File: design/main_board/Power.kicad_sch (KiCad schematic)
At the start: 45 parts, among them SW301 SW_SPDT, U301 AP2138N-3.3TRG1, U302 TPS61235P, U303 AAT3693

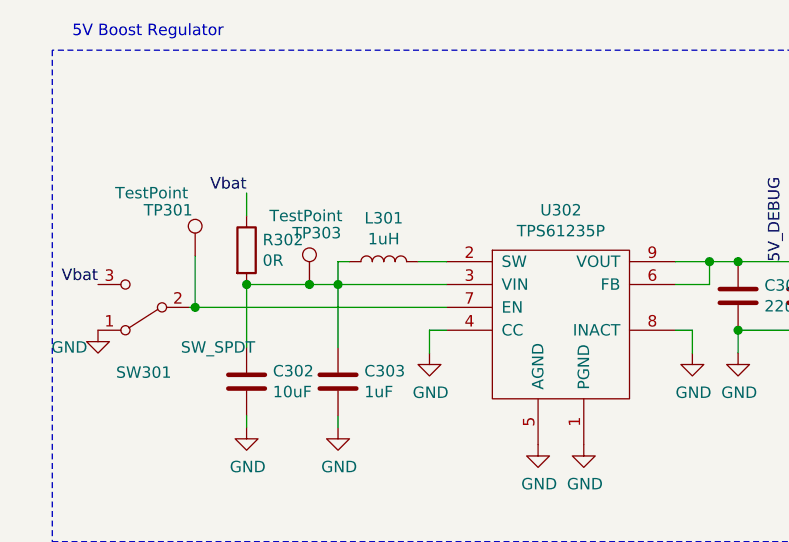
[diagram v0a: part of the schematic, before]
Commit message: Created esp32 footprint and symbol
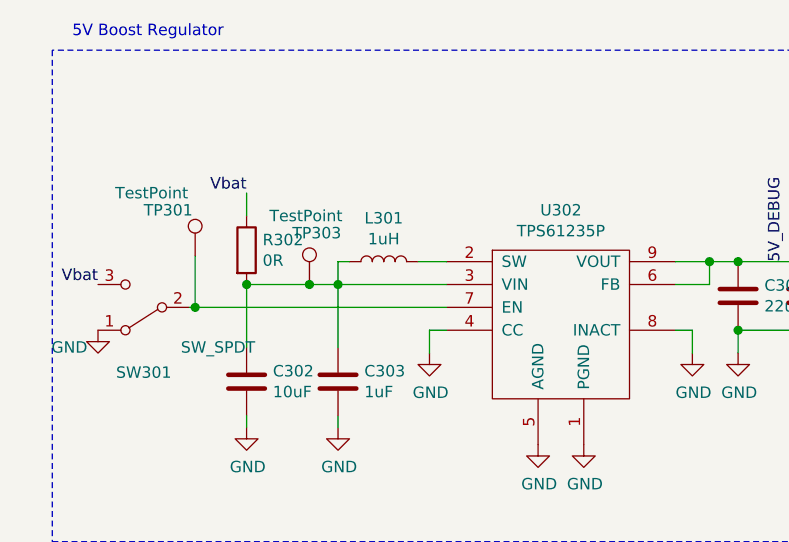
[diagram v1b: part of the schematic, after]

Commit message: Schematic almost finished
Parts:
- removed R301, R304, R306: 0R, Resistor_SMD:R_0603_1608Metric, symbol Device:R
- removed R302, R303, R307: 0R, Resistor_SMD:R_1206_3216Metric, symbol Device:R
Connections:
- net 3V3_DEBUG is gone; now on net +3V3: C305.1, D302.2 (A), TP304.1, U301.2 (Vout)
- net 5V_DEBUG is gone; now on net +5V: C304.1, C306.1, C307.1, D301.2 (A), TP305.1, U302.6 (FB), U302.9 (VOUT)
- net +5V: now also C301.1, TP302.1, U301.3 (Vin)
- net VBAT_SENSE: now also C302.1, C303.1, L301.1, TP303.1, U302.3 (VIN)
- net VBUS: now also C308.1, D303.2 (A), D304.2 (A), R313.1, TP306.1, U303.1 (VIN), U303.4 (EN)
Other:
- note removed: "Enable Resistor"

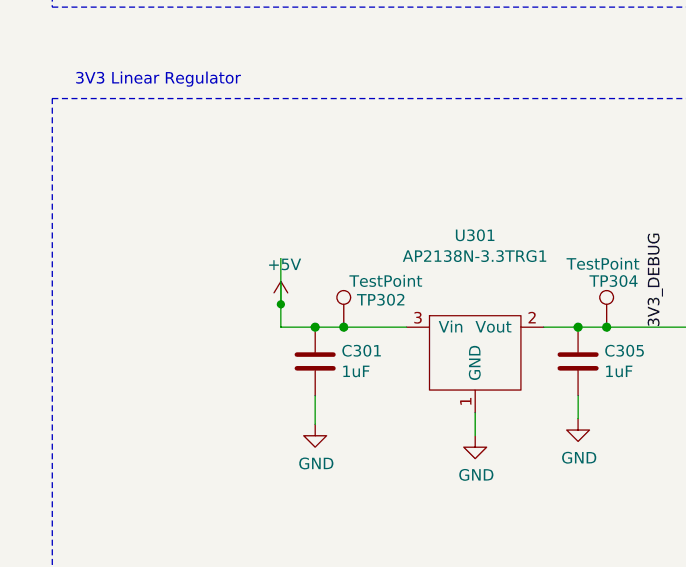
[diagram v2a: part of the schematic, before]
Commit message: Added new firmware hello world for ESP32-S3
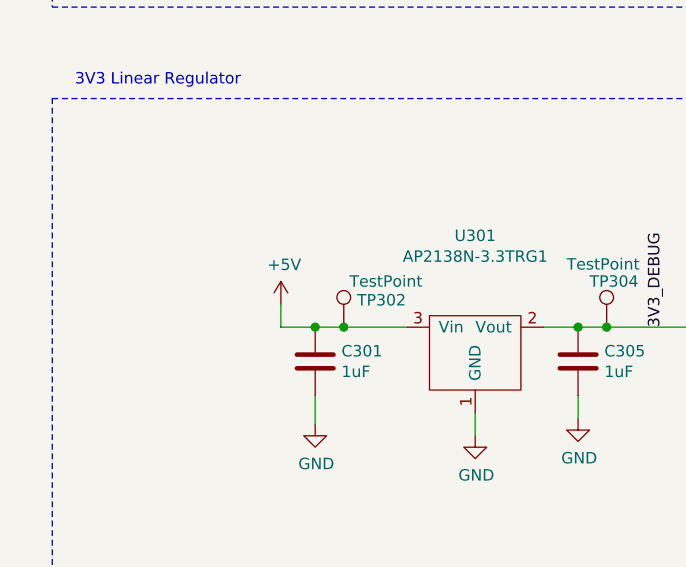
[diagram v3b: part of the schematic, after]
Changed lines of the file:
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@@
   (junction (at 100.33 53.975) (diameter 1.016) (color 0 0 0 0)
-  )
-  (junction (at 41.91 118.11) (diameter 0) (color 0 0 0 0)
   )
   (junction (at 102.87 53.975) (diameter 1.016) (color 0 0 0 0)
@@
     (stroke (width 0) (type solid) (color 0 0 0 0))
   )
-  (wire (pts (xy 41.91 113.03) (xy 41.91 118.11))
-    (stroke (width 0) (type default) (color 0 0 0 0))
-  )
   (wire (pts (xy 203.2 72.39) (xy 196.85 72.39))
